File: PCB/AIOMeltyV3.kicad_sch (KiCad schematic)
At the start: 30 parts, among them J1 USB4500-03-0-A_REVA1, SW1 Boot, SW2 Reset, U3 ESP32-S3-MINI-1, U4 RT9161A-33GV

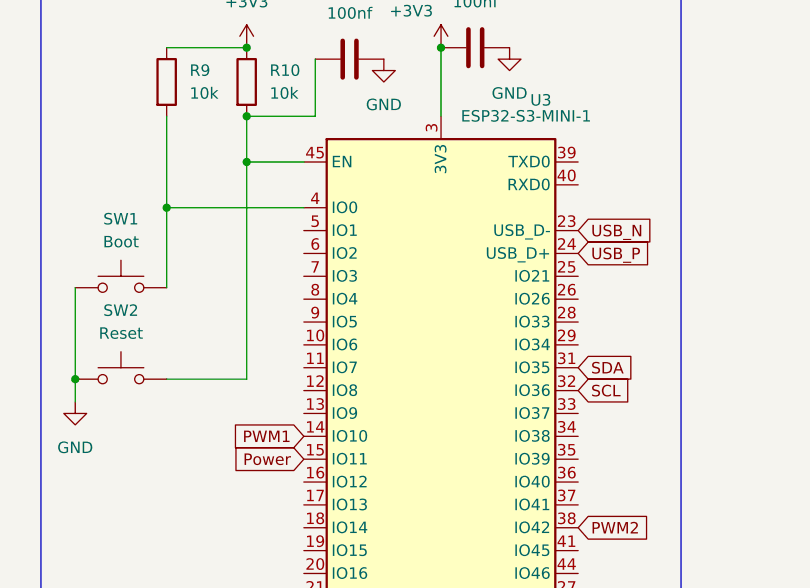
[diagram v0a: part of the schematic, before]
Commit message: Robot moves, I2C should now be on the correct pins
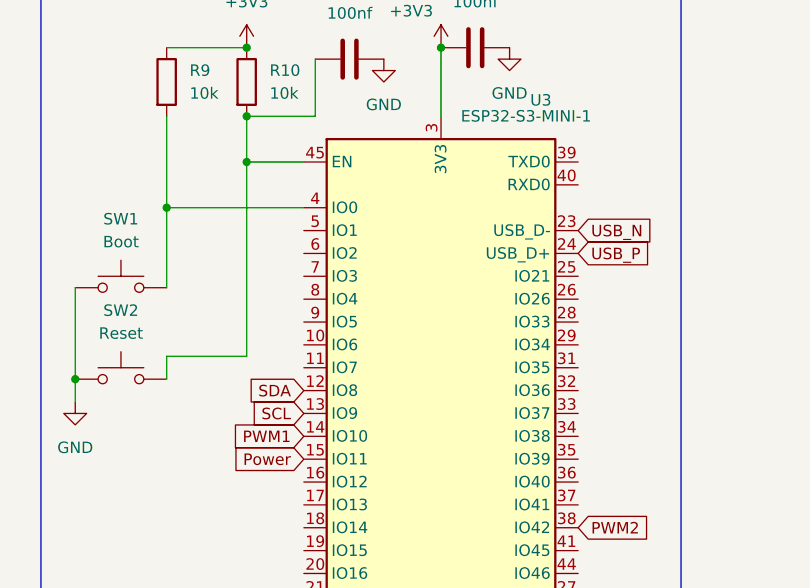
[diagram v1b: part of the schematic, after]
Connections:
- net SCL: now also U3.13 (IO9); no longer U3.32 (IO36)
- net SDA: now also U3.12 (IO8); no longer U3.31 (IO35)
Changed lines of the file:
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@@
 (kicad_sch
-	(version 20231120)
+	(version 20250114)
 	(generator "eeschema")
-	(generator_version "8.0")
+	(generator_version "9.0")
 	(paper "A4")
+	(rectangle
+		(start 16.51 13.97)
+		(end 80.01 128.27)
+		(stroke
+			(width 0)
+			(type default)
+		)
+		(fill
+			(type none)
+		)
+	)
+	(rectangle
+		(start 228.6 12.7)
+		(end 284.48 62.23)
+		(stroke
+			(width 0)
+			(type default)
+		)
+		(fill
+			(type none)
+		)
+	)
+	(rectangle
+		(start 105.41 34.29)
+		(end 176.53 125.73)
+		(stroke
+			(width 0)
+			(type default)
+		)
+		(fill
+			(type none)
+		)
+	)
+	(rectangle
+		(start 195.58 100.33)
+		(end 281.94 163.83)
+		(stroke
+			(width 0)
+			(type default)
+		)
+		(fill
+			(type none)
+		)
+	)
+	(rectangle
+		(start 13.97 152.4)
+		(end 101.6 190.5)
+		(stroke
+			(width 0)
+			(type default)
+		)
+		(fill
+			(type none)
+		)
+	)
+	(text "Power"
+		(exclude_from_sim no)
+		(at 16.764 150.876 0)
+		(effects
+			(font
+				(size 1.27 1.27)
+			)
+		)
+	)
+	(text "Acceleromiters"
+		(exclude_from_sim no)
+		(at 24.384 130.302 0)
+		(effects
+			(font
+				(size 1.27 1.27)
+			)
+		)
+	)
+	(text "USB"
+		(exclude_from_sim no)
+		(at 197.358 99.06 0)
+		(effects
+			(font
+				(size 1.27 1.27)
+			)
+		)
+	)
+	(text "All in one meltybrain control board"
+		(exclude_from_sim no)
+		(at 231.14 172.974 0)
+		(effects
+			(font
+				(face "KiCad Font")
+				(size 3.81 3.81)
+				(thickness 0.0406)
+				(bold yes)
+			)
+		)
+	)
+	(text "ESP32-S3"
+		(exclude_from_sim no)
+		(at 110.744 127.508 0)
+		(effects
+			(font
+				(size 1.27 1.27)
+			)
+		)
+	)
+	(text "Input Output"
+		(exclude_from_sim no)
+		(at 234.95 64.516 0)
+		(effects
+			(font
+				(size 1.27 1.27)
+			)
+		)
+	)
 	(junction
 		(at 63.5 54.61)
@@
 	(wire
 		(pts
-			(xy 128.27 85.09) (xy 128.27 60.96)
+			(xy 128.27 82.55) (xy 128.27 60.96)
 		)
 		(stroke
@@
 	(wire
 		(pts
+			(xy 119.38 82.55) (xy 119.38 85.09)
+		)
+		(stroke
+			(width 0)
+			(type default)
+		)
+	)
+	(wire
+		(pts
 			(xy 248.92 120.65) (xy 248.92 109.22)
 		)
@@
 	(wire
 		(pts
-			(xy 119.38 85.09) (xy 128.27 85.09)
+			(xy 119.38 82.55) (xy 128.27 82.55)
 		)
 		(stroke
@@
 		)
 	)
-	(rectangle
-		(start 16.51 13.97)
-		(end 80.01 128.27)
-		(stroke
-			(width 0)
-			(type default)
-		)
-		(fill
-			(type none)
-		)
-	)
-	(rectangle
-		(start 228.6 12.7)
-		(end 284.48 62.23)
-		(stroke
-			(width 0)
-			(type default)
-		)
-		(fill
-			(type none)
-		)
-	)
-	(rectangle
-		(start 105.41 34.29)
-		(end 176.53 125.73)
-		(stroke
-			(width 0)
-			(type default)
-		)
-		(fill
-			(type none)
-		)
-	)
-	(rectangle
-		(start 195.58 100.33)
-		(end 281.94 163.83)
-		(stroke
-			(width 0)
-			(type default)
-		)
-		(fill
-			(type none)
-		)
-	)
-	(rectangle
-		(start 13.97 152.4)
-		(end 101.6 190.5)
-		(stroke
-			(width 0)
-			(type default)
-		)
-		(fill
-			(type none)
-		)
-	)
-	(text "Power"
-		(exclude_from_sim no)
-		(at 16.764 150.876 0)
-		(effects
-			(font
-				(size 1.27 1.27)
-			)
-		)
-	)
-	(text "Acceleromiters"
-		(exclude_from_sim no)
-		(at 24.384 130.302 0)
-		(effects
-			(font
-				(size 1.27 1.27)
-			)
-		)
-	)
-	(text "USB"
-		(exclude_from_sim no)
-		(at 197.358 99.06 0)
-		(effects
-			(font
-				(size 1.27 1.27)
-			)
-		)
-	)
-	(text "All in one meltybrain control board"
-		(exclude_from_sim no)
-		(at 231.14 172.974 0)
-		(effects
-			(font
-				(face "KiCad Font")
-				(size 3.81 3.81)
-				(thickness 0.0406)
-				(bold yes)
-			)
-		)
-	)
-	(text "ESP32-S3"
-		(exclude_from_sim no)
-		(at 110.744 127.508 0)
-		(effects
-			(font
-				(size 1.27 1.27)
-			)
-		)
-	)
-	(text "Input Output"
-		(exclude_from_sim no)
-		(at 234.95 64.516 0)
-		(effects
-			(font
-				(size 1.27 1.27)
-			)
-		)
-	)
 	(global_label "PWM1"
 		(shape input)
@@
 	(global_label "SDA"
 		(shape input)
-		(at 165.1 83.82 0)
+		(at 134.62 86.36 180)
 		(fields_autoplaced yes)
 		(effects
@@
 				(size 1.27 1.27)
 			)
-			(justify left)
+			(justify right)
 		)
 		(property "Intersheetrefs" "${INTERSHEET_REFS}"
-			(at 171.6533 83.82 0)
+			(at 128.0667 86.36 0)
 			(effects
 				(font
 					(size 1.27 1.27)
 				)
-				(justify left)
+				(justify right)
 				(hide yes)
 			)
@@
 	(global_label "SCL"
 		(shape input)
-		(at 165.1 86.36 0)
+		(at 134.62 88.9 180)
 		(fields_autoplaced yes)
 		(effects
@@
 				(size 1.27 1.27)
 			)
-			(justify left)
+			(justify right)
 		)
 		(property "Intersheetrefs" "${INTERSHEET_REFS}"
-			(at 171.5928 86.36 0)
+			(at 128.1272 88.9 0)
 			(effects
 				(font
 					(size 1.27 1.27)
 				)
-				(justify left)
+				(justify right)
 				(hide yes)
 			)
@@
 		)
 	)
+	(embedded_fonts no)
 )

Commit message: I belive this is PIO updating librarys
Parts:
- added U5: DRV8833PW, Package_SO:TSSOP-16_4.4x5mm_P0.65mm, symbol Driver_Motor:DRV8833PW
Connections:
- net GND: now also U5.13 (GND)
- net PWM1: now also U5.16 (AIN1); no longer H1.MP
- net PWM2: now also U5.15 (AIN2); no longer H2.MP
- new net MotorL1: U5.2 (AOUT1)
- new net MotorL2: U5.4 (AOUT2)
- new net MotorR1: U5.7 (BOUT1)
- new net MotorR2: U5.5 (BOUT2)
- new net PWM3: U5.9 (BIN1)
- new net PWM4: U5.10 (BIN2)
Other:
- note added: "Speed Controler"
- moved on the sheet: C3, C5, R10, R9, SW1, SW2, U3
